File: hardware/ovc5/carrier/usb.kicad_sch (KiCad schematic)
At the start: 98 parts, among them J1 USB_C_Receptacle, U10 S25FL064, U2 CYUSB43x7, U5 USB3_A_Dual_Stacked, U8 TPS2561, Y1 25MHz

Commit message: Finish placement and routing
Signed-off-by: Luca Della Vedova <luca@openrobotics.org>
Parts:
- removed Y1: 25MHz, Crystal:Crystal_SMD_2016-4Pin_2.0x1.6mm, symbol Device:Crystal_Small
- added Y1: 25MHz, Crystal:Crystal_SMD_2016-4Pin_2.0x1.6mm, symbol Device:Crystal_GND24_Small
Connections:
- net +3V3: now also U2.M7 (VBUS)
- net +5V: no longer U2.M7 (VBUS)
- net at C63.2, U2.A6 (XIN): now also Y1.1
- net at C64.1, U2.A7 (XOUT): now also Y1.3
- no-connect marks 54 -> 56
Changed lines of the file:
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@@
   (junction (at 95.25 -5.08) (diameter 0.9144) (color 0 0 0 0))
   (junction (at 95.25 0) (diameter 0.9144) (color 0 0 0 0))
-  (junction (at 95.25 116.84) (diameter 0.9144) (color 0 0 0 0))
-  (junction (at 95.25 121.92) (diameter 0.9144) (color 0 0 0 0))
+  (junction (at 96.52 116.84) (diameter 0.9144) (color 0 0 0 0))
+  (junction (at 96.52 121.92) (diameter 0.9144) (color 0 0 0 0))
   (junction (at 96.52 173.99) (diameter 0.9144) (color 0 0 0 0))
   (junction (at 97.79 -21.59) (diameter 0.9144) (color 0 0 0 0))
@@
   (no_connect (at 55.88 111.76))
   (no_connect (at 55.88 114.3))
+  (no_connect (at 93.98 119.38))
+  (no_connect (at 99.06 119.38))
   (no_connect (at 105.41 77.47))
   (no_connect (at 105.41 80.01))
@@
     (stroke (width 0) (type solid) (color 0 0 0 0))
   )
-  (wire (pts (xy 91.44 116.84) (xy 95.25 116.84))
+  (wire (pts (xy 91.44 116.84) (xy 96.52 116.84))
     (stroke (width 0) (type solid) (color 0 0 0 0))
   )
-  (wire (pts (xy 91.44 121.92) (xy 95.25 121.92))
+  (wire (pts (xy 91.44 121.92) (xy 96.52 121.92))
     (stroke (width 0) (type solid) (color 0 0 0 0))
   )
@@
     (stroke (width 0) (type solid) (color 0 0 0 0))
   )
-  (wire (pts (xy 95.25 116.84) (xy 104.14 116.84))
+  (wire (pts (xy 96.52 116.84) (xy 104.14 116.84))
     (stroke (width 0) (type solid) (color 0 0 0 0))
   )
-  (wire (pts (xy 95.25 121.92) (xy 104.14 121.92))
+  (wire (pts (xy 96.52 121.92) (xy 104.14 121.92))
     (stroke (width 0) (type solid) (color 0 0 0 0))
   )
@@
     (pin "1")
   )
-  (symbol (lib_id "power:+5V") (at 7.62 99.06 0) (unit 1)
+  (symbol (lib_id "power:+3V3") (at 7.62 99.06 0) (unit 1)
     (in_bom yes) (on_board yes)
     (property "Reference" "#PWR0166" (id 0) (at 7.62 102.87 0)
       (effects (font (size 1.27 1.27)) hide)
     )
-    (property "Value" "+5V" (id 1) (at 8.89 93.98 0))
+    (property "Value" "+3V3" (id 1) (at 8.89 93.98 0))
     (property "Footprint" "" (id 2) (at 7.62 99.06 0)
       (effects (font (size 1.27 1.27)) hide)
@@
     (pin "2")
   )
-  (symbol (lib_id "Device:Crystal_Small") (at 95.25 119.38 270) (unit 1)
-    (in_bom yes) (on_board yes)
-    (property "Reference" "Y1" (id 0) (at 97.79 118.11 90)
-      (effects (font (size 1.27 1.27)) (justify left))
-    )
-    (property "Value" "25MHz" (id 1) (at 97.79 120.65 90)
-      (effects (font (size 1.27 1.27)) (justify left))
-    )
-    (property "Footprint" "Crystal:Crystal_SMD_2016-4Pin_2.0x1.6mm" (id 2) (at 95.25 119.38 0)
-      (effects (font (size 1.27 1.27)) hide)
-    )
-    (property "Datasheet" "~" (id 3) (at 95.25 119.38 0)
-      (effects (font (size 1.27 1.27)) hide)
-    )
-    (pin "1")
-    (pin "2")
-  )
   (symbol (lib_id "Device:C_Small") (at 31.75 -2.54 0) (unit 1)
     (in_bom yes) (on_board yes)
@@
     (pin "2")
   )
+  (symbol (lib_id "Device:Crystal_GND24_Small") (at 96.52 119.38 270) (unit 1)
+    (in_bom yes) (on_board yes)
+    (property "Reference" "Y1" (id 0) (at 93.98 114.3 90)
+      (effects (font (size 1.27 1.27)) (justify left))
+    )
+    (property "Value" "25MHz" (id 1) (at 96.52 114.3 90)
+      (effects (font (size 1.27 1.27)) (justify left))
+    )
+    (property "Footprint" "Crystal:Crystal_SMD_2016-4Pin_2.0x1.6mm" (id 2) (at 96.52 119.38 0)
+      (effects (font (size 1.27 1.27)) hide)
+    )
+    (property "Datasheet" "~" (id 3) (at 96.52 119.38 0)
+      (effects (font (size 1.27 1.27)) hide)
+    )
+    (pin "1")
+    (pin "2")
+    (pin "3")
+    (pin "4")
+  )
   (symbol (lib_id "Device:D_TVS_Dual_AAC") (at 234.95 203.2 90) (unit 1)
     (in_bom yes) (on_board yes)
@@
     )
     (pin "1")
-    (pin "2")
-    (pin "3")
-    (pin "4")
-    (pin "5")
-    (pin "6")
-    (pin "7")
-    (pin "8")
-    (pin "9")
     (pin "10")
     (pin "11")
@@
     (pin "17")
     (pin "18")
+    (pin "2")
+    (pin "3")
+    (pin "4")
+    (pin "5")
+    (pin "6")
+    (pin "7")
+    (pin "8")
+    (pin "9")
     (pin "S")
   )
@@
       (effects (font (size 1.27 1.27)) hide)
     )
-    (pin "K7")
-    (pin "M6")
-    (pin "J5")
-    (pin "H5")
     (pin "A10")
-    (pin "B10")
-    (pin "F12")
-    (pin "D12")
-    (pin "E11")
-    (pin "D11")
-    (pin "A9")
-    (pin "B9")
-    (pin "M5")
-    (pin "G10")
-    (pin "P7")
-    (pin "N7")
     (pin "A11")
-    (pin "B11")
-    (pin "B12")
-    (pin "E12")
-    (pin "E5")
-    (pin "A8")
-    (pin "E3")
-    (pin "K5")
-    (pin "C8")
     (pin "A6")
     (pin "A7")
-    (pin "M9")
-    (pin "M8")
+    (pin "A8")
+    (pin "A9")
+    (pin "B10")
+    (pin "B11")
+    (pin "B12")
+    (pin "B4")
+    (pin "B9")
+    (pin "C10")
     (pin "C11")
-    (pin "K4")
+    (pin "C8")
     (pin "D10")
-    (pin "C10")
-    (pin "B4")
+    (pin "D11")
+    (pin "D12")
+    (pin "E10")
+    (pin "E11")
+    (pin "E12")
+    (pin "E3")
+    (pin "E5")
+    (pin "F12")
     (pin "F3")
+    (pin "G10")
+    (pin "H5")
+    (pin "J5")
     (pin "K11")
-    (pin "E10")
+    (pin "K4")
+    (pin "K5")
+    (pin "K7")
     (pin "M10")
+    (pin "M5")
+    (pin "M6")
+    (pin "M8")
+    (pin "M9")
+    (pin "N7")
+    (pin "P7")
   )
   (symbol (lib_id "usb_controller:CYUSB43x7") (at 187.96 99.06 0) (unit 3)
@@
       (effects (font (size 1.27 1.27)) hide)
     )
-    (pin "K8")
-    (pin "E8")
-    (pin "F4")
-    (pin "F11")
-    (pin "J11")
-    (pin "J4")
-    (pin "N10")
-    (pin "D9")
+    (pin "A5")
     (pin "B6")
-    (pin "C3")
     (pin "C12")
-    (pin "L10")
-    (pin "J12")
-    (pin "C9")
-    (pin "A5")
-    (pin "N5")
-    (pin "N4")
-    (pin "L4")
-    (pin "M4")
-    (pin "J3")
-    (pin "H3")
-    (pin "H12")
-    (pin "H11")
-    (pin "M12")
-    (pin "L11")
-    (pin "K12")
-    (pin "K3")
-    (pin "G11")
-    (pin "G4")
-    (pin "P8")
-    (pin "N8")
-    (pin "P9")
-    (pin "N9")
-    (pin "P4")
-    (pin "P5")
-    (pin "P6")
-    (pin "N6")
-    (pin "P10")
-    (pin "L3")
-    (pin "G3")
-    (pin "G12")
-    (pin "L12")
-    (pin "M3")
+    (pin "C3")
     (pin "C4")
+    (pin "C9")
     (pin "D7")
+    (pin "D9")
     (pin "E7")
+    (pin "E8")
+    (pin "F11")
+    (pin "F4")
     (pin "F6")
     (pin "F7")
     (pin "F8")
     (pin "F9")
+    (pin "G11")
+    (pin "G12")
+    (pin "G3")
+    (pin "G4")
     (pin "G6")
     (pin "G7")
     (pin "G8")
     (pin "G9")
+    (pin "H11")
+    (pin "H12")
+    (pin "H3")
     (pin "H6")
     (pin "H7")
     (pin "H8")
     (pin "H9")
+    (pin "J11")
+    (pin "J12")
+    (pin "J3")
+    (pin "J4")
     (pin "J7")
     (pin "J8")
     (pin "J9")
+    (pin "K12")
+    (pin "K3")
+    (pin "K8")
+    (pin "L10")
+    (pin "L11")
+    (pin "L12")
+    (pin "L3")
+    (pin "L4")
+    (pin "M12")
+    (pin "M3")
+    (pin "M4")
+    (pin "N10")
+    (pin "N4")
+    (pin "N5")
+    (pin "N6")
+    (pin "N8")
+    (pin "N9")
+    (pin "P10")
+    (pin "P4")
+    (pin "P5")
+    (pin "P6")
+    (pin "P8")
+    (pin "P9")
   )
   (symbol (lib_id "usb_controller:CYUSB43x7") (at 35.56 101.6 0) (unit 1)
@@
       (effects (font (size 1.27 1.27)) hide)
     )
-    (pin "K2")
-    (pin "K1")
-    (pin "L1")
-    (pin "L2")
-    (pin "M1")
-    (pin "M2")
-    (pin "P3")
-    (pin "P2")
-    (pin "N2")
-    (pin "N1")
-    (pin "B2")
+    (pin "A12")
+    (pin "A13")
+    (pin "A2")
+    (pin "A3")
+    (pin "A4")
     (pin "B1")
+    (pin "B13")
+    (pin "B14")
+    (pin "B2")
+    (pin "B3")
+    (pin "B5")
+    (pin "B7")
+    (pin "B8")
     (pin "C1")
+    (pin "C13")
+    (pin "C14")
     (pin "C2")
+    (pin "C5")
+    (pin "C6")
+    (pin "C7")
     (pin "D1")
+    (pin "D13")
+    (pin "D14")
     (pin "D2")
-    (pin "F2")
-    (pin "F1")
-    (pin "E2")
+    (pin "D3")
+    (pin "D4")
+    (pin "D5")
+    (pin "D6")
+    (pin "D8")
     (pin "E1")
-    (pin "B14")
-    (pin "B13")
-    (pin "F14")
-    (pin "F13")
-    (pin "E14")
     (pin "E13")
-    (pin "C13")
-    (pin "C14")
-    (pin "D13")
-    (pin "D14")
-    (pin "K14")
-    (pin "K13")
-    (pin "P12")
-    (pin "P13")
-    (pin "N13")
-    (pin "N14")
-    (pin "L13")
-    (pin "L14")
-    (pin "M13")
-    (pin "M14")
-    (pin "J14")
-    (pin "J13")
-    (pin "H14")
-    (pin "H13")
-    (pin "G14")
-    (pin "G13")
-    (pin "J1")
-    (pin "J2")
+    (pin "E14")
+    (pin "E2")
+    (pin "E4")
+    (pin "E6")
+    (pin "E9")
+    (pin "F1")
+    (pin "F10")
+    (pin "F13")
+    (pin "F14")
+    (pin "F2")
+    (pin "F5")
     (pin "G1")
+    (pin "G13")
+    (pin "G14")
     (pin "G2")
+    (pin "G5")
     (pin "H1")
+    (pin "H10")
+    (pin "H13")
+    (pin "H14")
     (pin "H2")
-    (pin "A13")
-    (pin "A12")
-    (pin "A3")
-    (pin "A2")
+    (pin "H4")
+    (pin "J1")
+    (pin "J10")
+    (pin "J13")
+    (pin "J14")
+    (pin "J2")
+    (pin "J6")
+    (pin "K1")
+    (pin "K10")
+    (pin "K13")
+    (pin "K14")
+    (pin "K2")
     (pin "K6")
-    (pin "F10")
-    (pin "N12")
-    (pin "L7")
+    (pin "K9")
+    (pin "L1")
+    (pin "L13")
+    (pin "L14")
+    (pin "L2")
     (pin "L5")
-    (pin "H10")
+    (pin "L6")
+    (pin "L7")
+    (pin "L8")
+    (pin "L9")
+    (pin "M1")
     (pin "M11")
-    (pin "J6")
-    (pin "E9")
+    (pin "M13")
+    (pin "M14")
+    (pin "M2")
+    (pin "M7")
+    (pin "N1")
     (pin "N11")
+    (pin "N12")
+    (pin "N13")
+    (pin "N14")
+    (pin "N2")
     (pin "N3")
-    (pin "L6")
-    (pin "J10")
     (pin "P11")
-    (pin "M7")
-    (pin "D4")
-    (pin "E4")
-    (pin "H4")
-    (pin "E6")
-    (pin "B5")
-    (pin "D6")
-    (pin "C5")
-    (pin "A4")
-    (pin "D3")
-    (pin "D8")
-    (pin "K9")
-    (pin "L8")
-    (pin "B3")
-    (pin "C7")
-    (pin "K10")
-    (pin "L9")
-    (pin "G5")
-    (pin "C6")
-    (pin "D5")
-    (pin "F5")
-    (pin "B7")
-    (pin "B8")
+    (pin "P12")
+    (pin "P13")
+    (pin "P2")
+    (pin "P3")
   )
 )

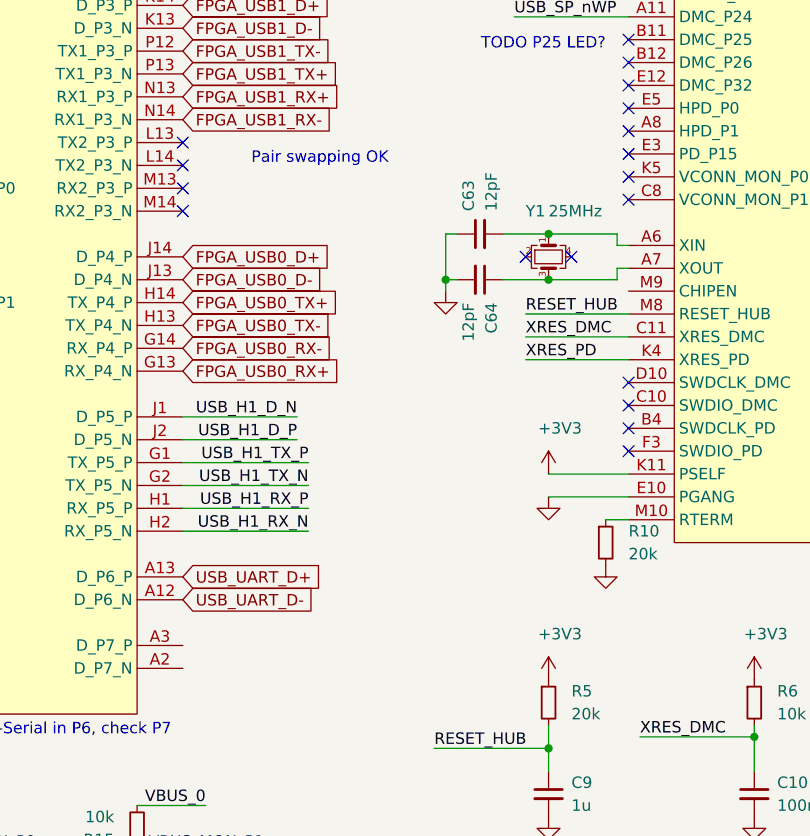
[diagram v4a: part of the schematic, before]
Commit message: Add parts for BOM
Signed-off-by: Luca Della Vedova <luca@openrobotics.org>
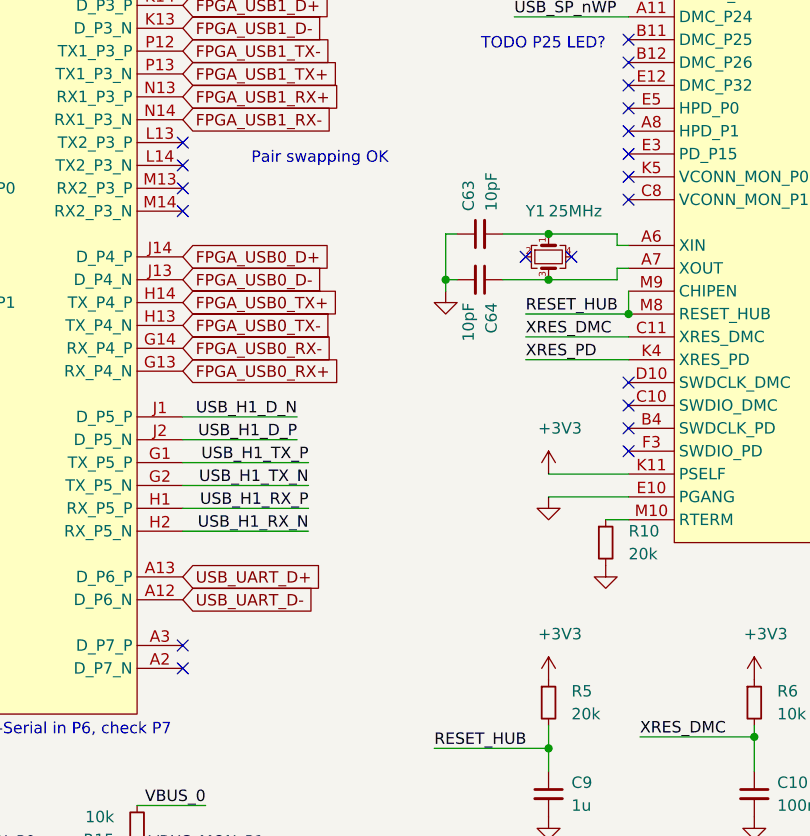
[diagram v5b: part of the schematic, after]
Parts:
- C1, C10, C11, C12, C13, C14, C15, C16, C17, C18, C19, C20, C21, C22, C24, C30, C32, C36, C37, C38, C39, C40, C41, C42, C43, C44, C45, C48, C49, C50, C52, C53, C54, C56, C57, C59, C60, C61, C65, C66, C67, C68, C70, C74, C75, C76, C77, C79, C80, C81, C82: D1N (none) -> Digikey; D1PN (none) -> 1276-1043-1-ND; MFN (none) -> Samsung; MPN (none) -> CL05A104KA5NNNC
- C25, C34, C47: D1N (none) -> Digikey; D1PN (none) -> 1276-6830-1-ND; MFN (none) -> Samsung; MPN (none) -> CL05A106MP8NUB8
- C26, C27, C28, C46, C51: D1N (none) -> Digikey; D1PN (none) -> 1276-1051-1-ND; MFN (none) -> Samsung; MPN (none) -> CL05B103KO5NNNC
- C29, C31, C62: D1N (none) -> Digikey; D1PN (none) -> 587-3408-1-ND; MFN (none) -> Taiyo Yuden; MPN (none) -> LMK105BBJ475MVLF
- C33, C35, C55, C58, C9: D1N (none) -> Digikey; D1PN (none) -> 1276-1076-1-ND; MFN (none) -> Samsung; MPN (none) -> CL05A105KP5NNNC
- C63, C64: value 12pF -> 10pF; D1N (none) -> Digikey; D1PN (none) -> 587-1947-1-ND; MFN (none) -> Taiyo Yuden; MPN (none) -> UMK105CG100DV-F
- C69, C71: D1N (none) -> Digikey; D1PN (none) -> 445-6007-1-ND; MFN (none) -> TDK; MPN (none) -> C3216X5R1A107M160AC
- D3, D4, D5: D1N (none) -> Digikey; D1PN (none) -> 296-25509-1-ND; MFN (none) -> TI; MPN (none) -> TPD2EUSB30DRTR
- J1: D1N (none) -> Digikey; D1PN (none) -> 732-9618-1-ND; MFN (none) -> Wurth; MPN (none) -> 632723300011
- R1: D1N (none) -> Digikey; D1PN (none) -> 311-47.0KLRCT-ND; MFN (none) -> Yageo; MPN (none) -> RC0402FR-0747KL
- R10, R5: D1N (none) -> Digikey; D1PN (none) -> 311-20.0KLRCT-ND; MFN (none) -> Yageo; MPN (none) -> RC0402FR-0720KL
- R11, R12, R8, R9: D1N (none) -> Digikey; D1PN (none) -> YAG3515CT-ND; MFN (none) -> Yageo; MPN (none) -> YAG3515CT-ND
- R13, R15, R44, R6, R7: D1N (none) -> Digikey; D1PN (none) -> YAG3436CT-ND; MFN (none) -> Yageo; MPN (none) -> AC0402FR-0710KL
- R14, R16: D1N (none) -> Digikey; D1PN (none) -> RR05P1.0KDCT-ND; MFN (none) -> Susumu; MPN (none) -> RR0510P-102-D
- R19, R20: D1N (none) -> Digikey; D1PN (none) -> RR05P5.1KDCT-ND; MFN (none) -> Susumu; MPN (none) -> RR0510P-512-D
- U10: D1N (none) -> Digikey; D1PN (none) -> 428-4640-1-ND; MFN (none) -> Cypress; MPN (none) -> S25FL064LABNFI013
- U2: D1N (none) -> Arrow; D1PN (none) -> CYUSB4347-BZXCES; MFN (none) -> Cypress; MPN (none) -> CYUSB4347-BZXCES
- U5: D1N (none) -> Digikey; D1PN (none) -> WM10420-ND; MFN (none) -> Molex; MPN (none) -> 0484060003
- U8: D1N (none) -> Digikey; D1PN (none) -> 296-37670-1-ND; MFN (none) -> TI; MPN (none) -> TPS2561DRCR
- Y1: D1N (none) -> Digikey; D1PN (none) -> 535-13851-1-ND; MFN (none) -> Abracon; MPN (none) -> ABM11W-25.0000MHZ-7-K1Z-T3
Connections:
- net RESET_HUB: now also U2.M9 (CHIPEN)
- no-connect marks 56 -> 58
